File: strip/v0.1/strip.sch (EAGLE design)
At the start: 96 parts, among them IC1 LP2992, IC2 ADP3110A-SO8, IC4 OPA335, IC5 ADP3110A-SO8, IC6 ADP3110A-SO8, IC7 STM32F050CX, Q1 IRF7828, Q2 IRF7828, Q3 IRF7828, Q4 IRF7828, Q5 IRF7828, Q6 IRF7828

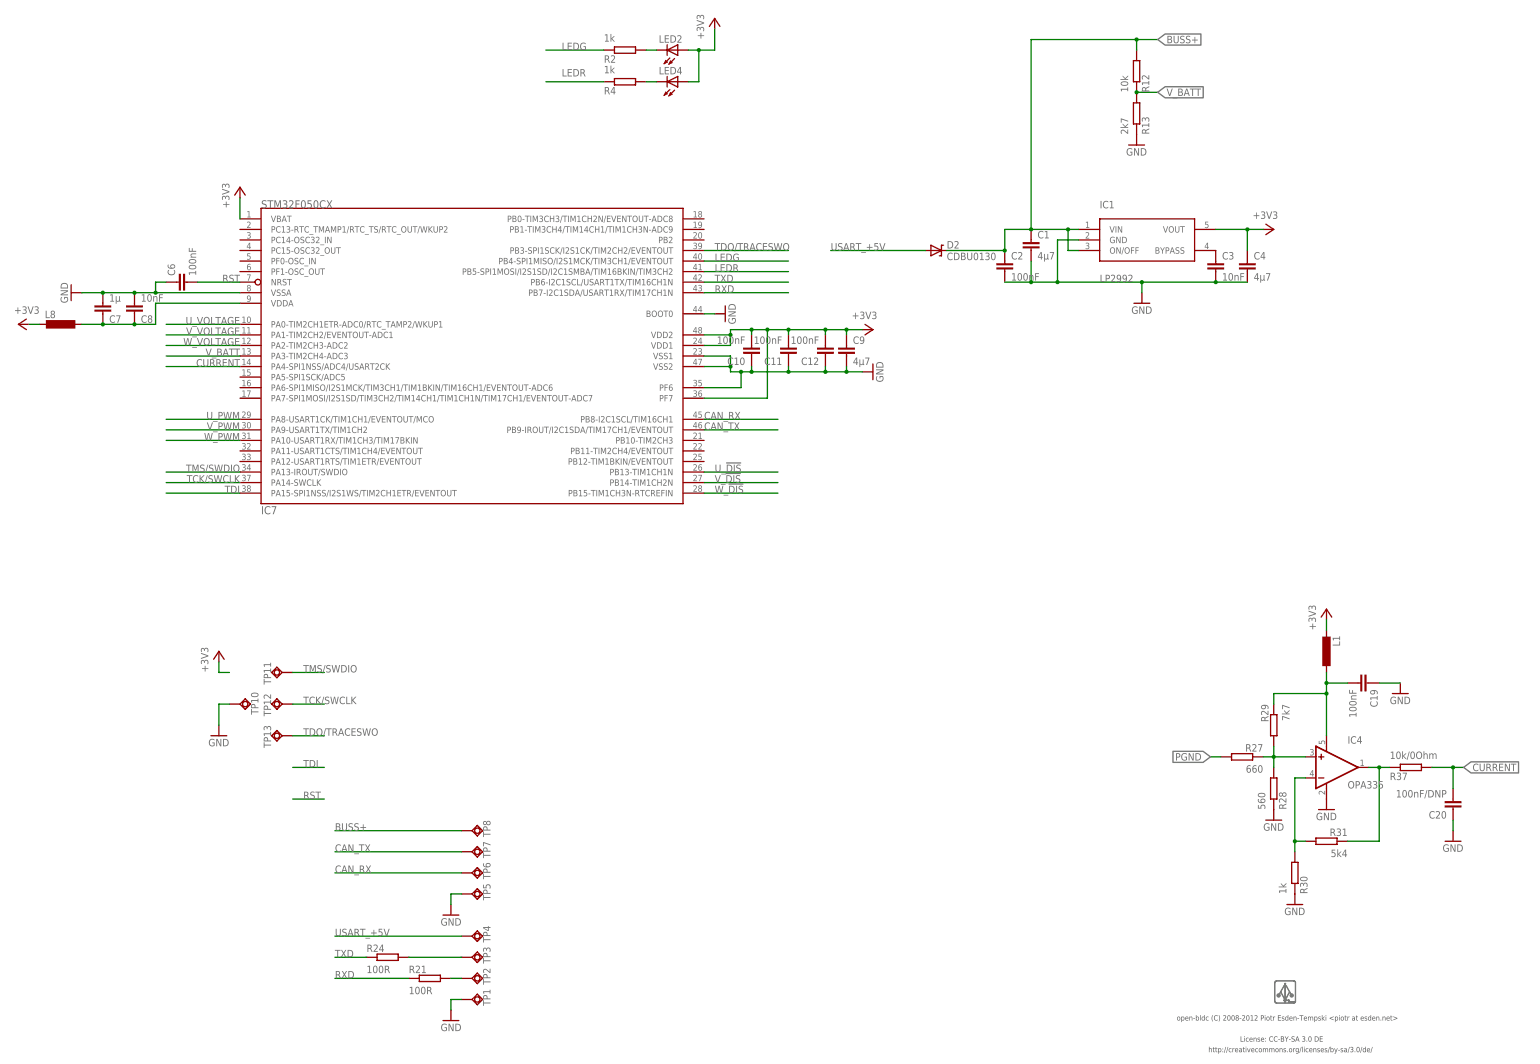
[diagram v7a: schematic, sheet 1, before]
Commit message: Added 3v3 CAN transceiver footprint to the strip.
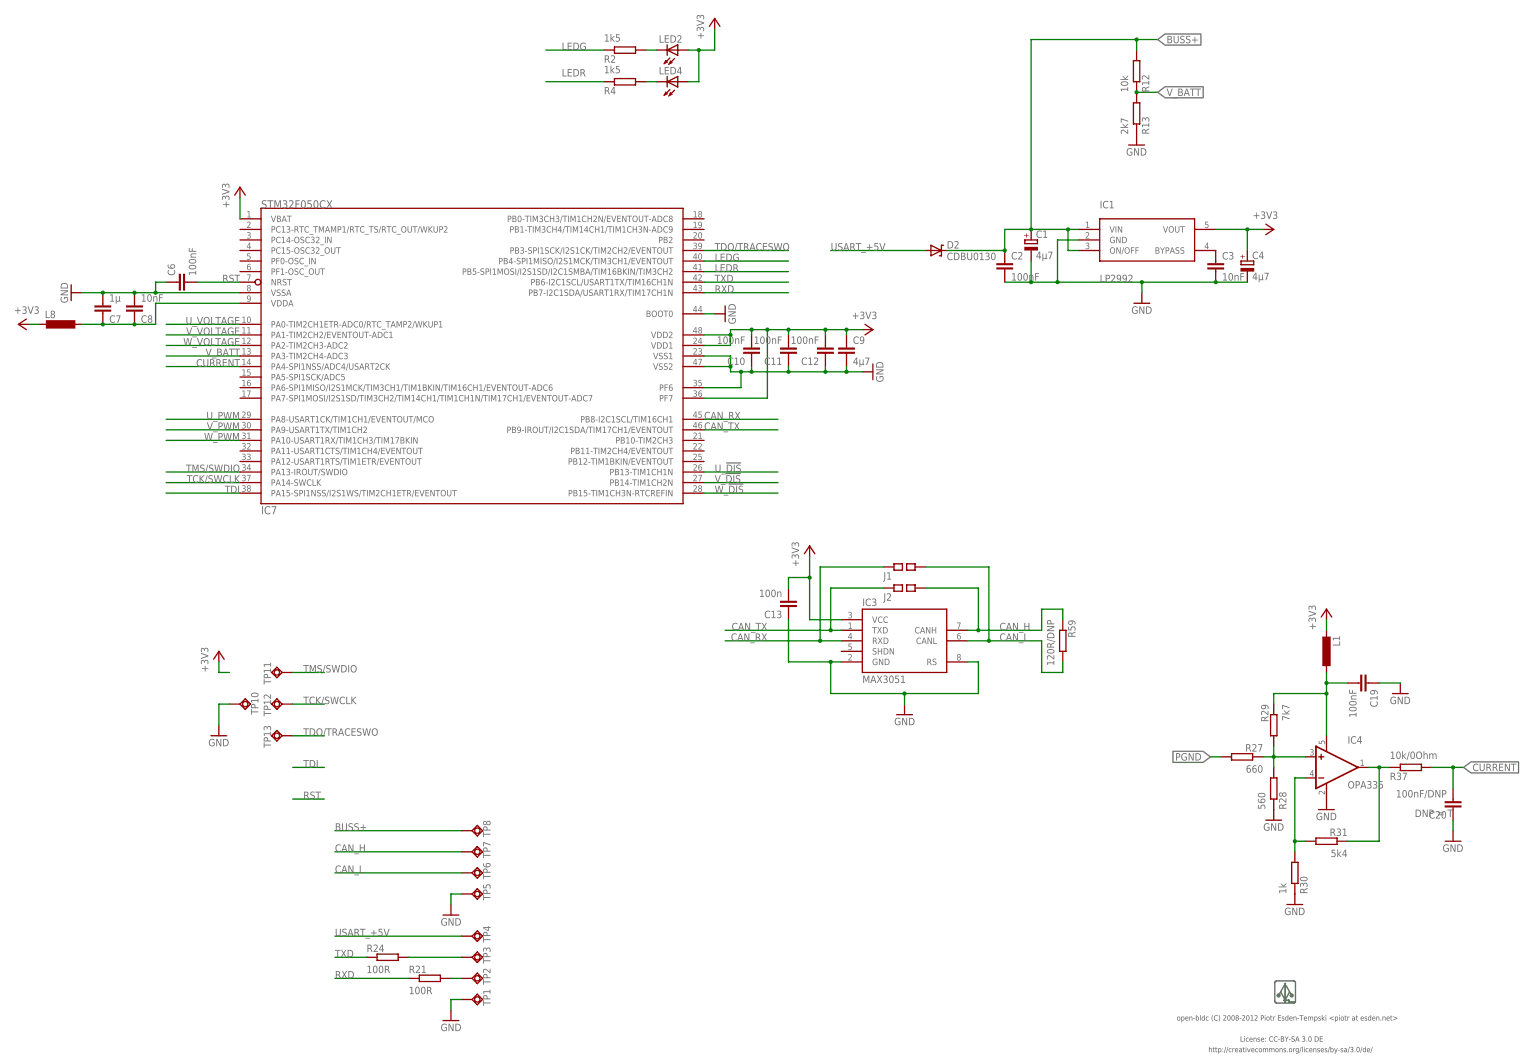
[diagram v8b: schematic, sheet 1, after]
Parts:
- added C13: 100n, pel_dipol_comp:CAPACITOR-0402
- added IC3: MAX3051, open-bldc:MAX3051
- added J1, J2: (no value), pel_jumpers:SQ_JMP-0402
- added R59: 120R/DNP, pel_dipol_comp:RESISTOR-0402
- C1, C4: device pel_dipol_comp:CAPACITOR-0402 -> pel_dipol_comp:CAPACITOR-POL-0805; PARTNO (none) -> cap-cer-0805-4u7-16v
- C10, C11, C12, C19, C2, C6: PARTNO (none) -> cap-cer-0402-100n
- C20: DNP (none) -> T; PARTNO (none) -> cap-cer-0402-100n
- C23, C24, C25: PARTNO (none) -> cap-tan-0603-1u
- C26, C27, C32: value 100n -> 100nF; PARTNO (none) -> cap-cer-0402-100n
- C3, C8: PARTNO (none) -> cap-cer-0402-10n
- C5: value (none) -> 220uF; PARTNO (none) -> cap-tan-D-220u-16v
- C7: PARTNO (none) -> cap-cer-0402-1u
- C9: PARTNO (none) -> cap-cer-0805-4u7
- D1, D3, D4, L2, L3, L4, L5, L6, L7, PAD1, PAD2, PAD3, PAD4, PAD5, R15, R17, R22, U$1, U$2: PARTNO (none) -> *
- D2: PARTNO (none) -> diode-0603
- IC1: PARTNO (none) -> vreg-sot-23-5-3v3
- IC2, IC5, IC6: PARTNO (none) -> ic-so8-mosfet-driver-buck
- IC4: PARTNO (none) -> ic-sot-23-5-opamp
- IC7: PARTNO (none) -> mcu-tqfp-32-stm32f05
- L1, L8: PARTNO (none) -> ferrite-0603-600ohm
- LED2, LED4: PARTNO (none) -> led-0402-green
- Q1, Q2, Q3, Q4, Q5, Q6: PARTNO (none) -> ic-so8-mosfet-n-ch-30v-15a
- R10, R2, R4, R5, R6, R7, R8, R9: value 1k -> 1k5; PARTNO (none) -> res-0402-1k5
- R12, R14, R16, R18: PARTNO (none) -> res-0402-10k
- R13: PARTNO (none) -> res-0402-2k7
- R21, R24: PARTNO (none) -> res-0402-100
- R27: PARTNO (none) -> res-0402-665
- R28: PARTNO (none) -> res-0402-560
- R29: PARTNO (none) -> res-0402-7k68
- R30: PARTNO (none) -> res-0402-1k
- R31: PARTNO (none) -> res-0402-5k36
- R37: PARTNO (none) -> res-0402-0
- R45: value 0.05Ohm -> 0.005Ohm; PARTNO (none) -> res-1206-0005
- R46, R47, R48, R49, R50, R51: PARTNO (none) -> res-0402-10
- TP1, TP10, TP11, TP12, TP13, TP2, TP3, TP4, TP5, TP6, TP7, TP8: DNP (none) -> T; PARTNO (none) -> *
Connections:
- new net CAN_H: IC3.CANH, J2.2, R59.1, TP7.TP
- new net CAN_L: IC3.CANL, J1.2, R59.2, TP6.TP
- net +3V3: now also C13.2, C4.+, IC3.VCC; no longer C4.1
- net BUSS+: now also C1.+; no longer C1.1
- net CAN_RX: now also IC3.RXD, J1.1; no longer TP6.TP
- net CAN_TX: now also IC3.TXD, J2.1; no longer TP7.TP
- net GND: now also C1.-, C13.1, C4.-, IC3.GND, IC3.RS; no longer C1.2, C4.2
